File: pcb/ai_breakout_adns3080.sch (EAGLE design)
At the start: 24 parts, among them J1 1X10, U1 VREG-MIC5205-3.3, U2 ADNS-3080, X1 RESON

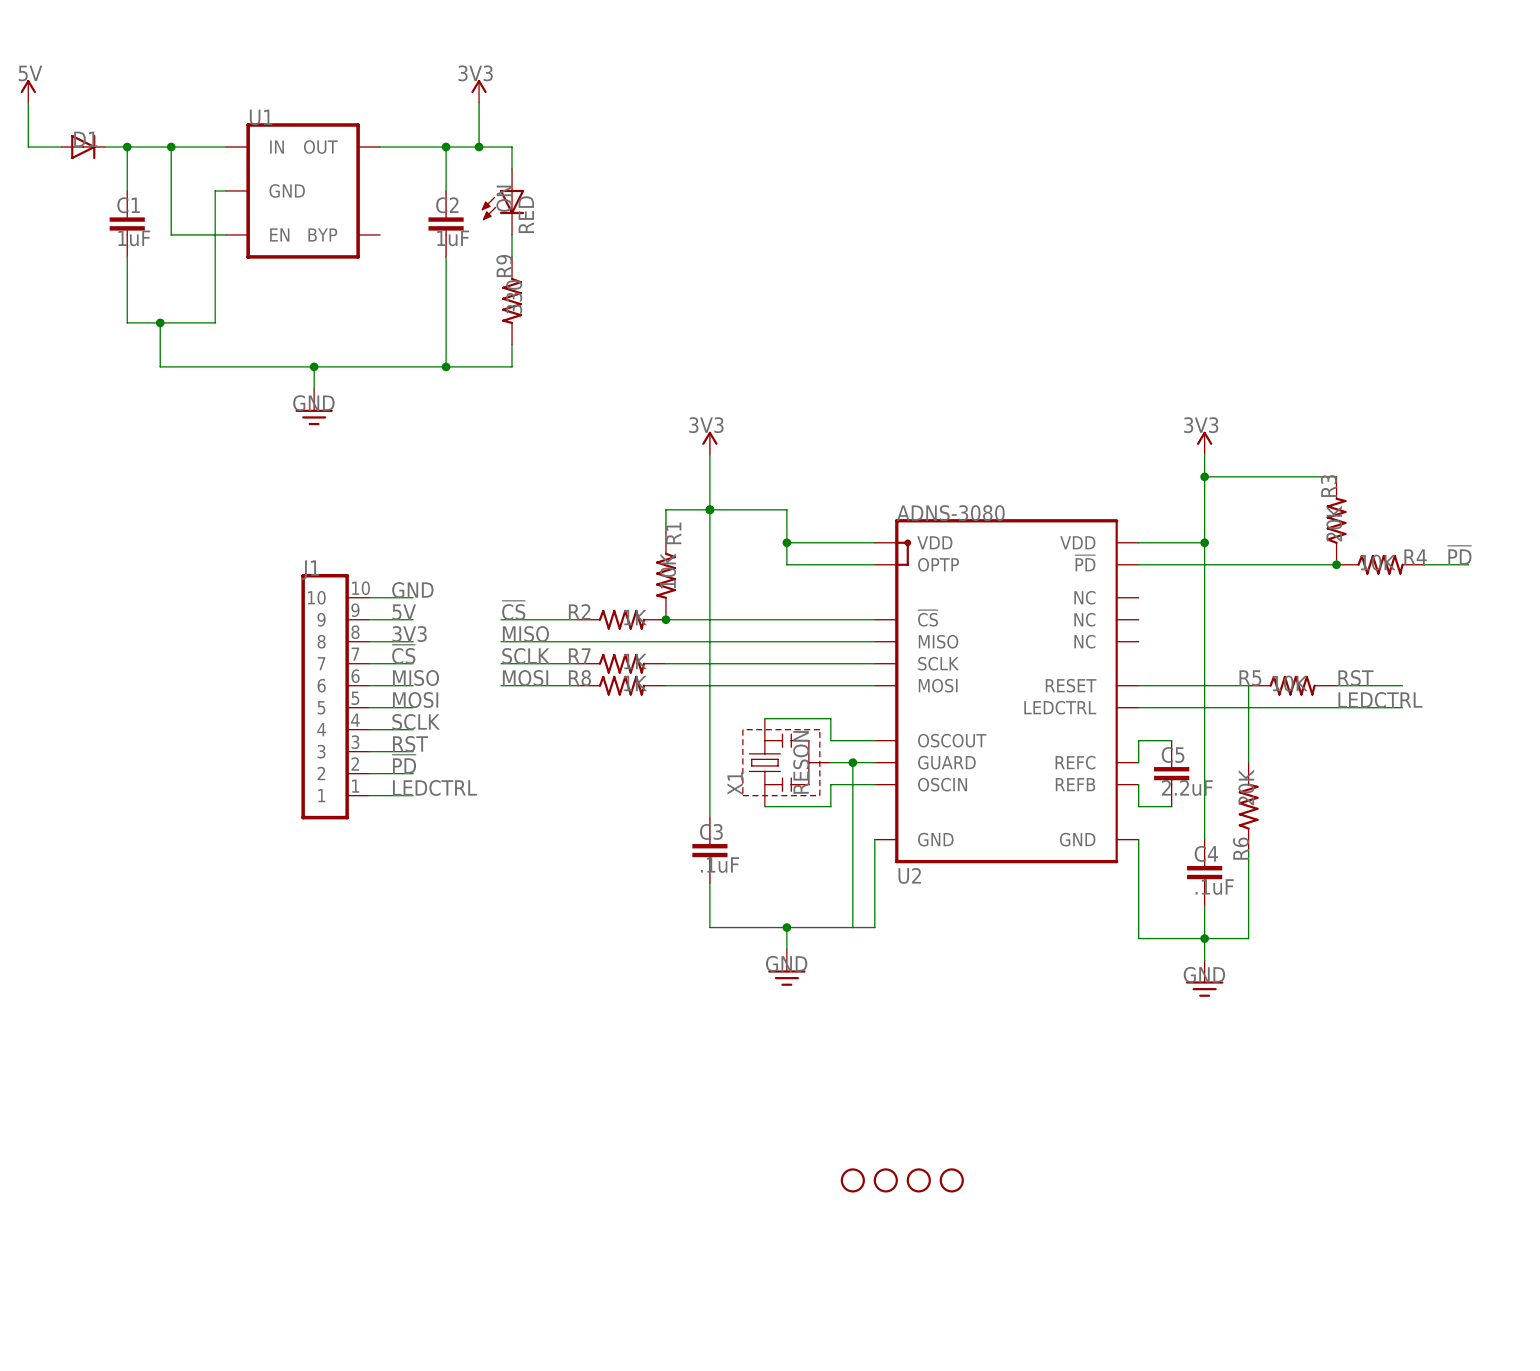
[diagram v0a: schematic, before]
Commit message: Revised version.  Finished BOM.
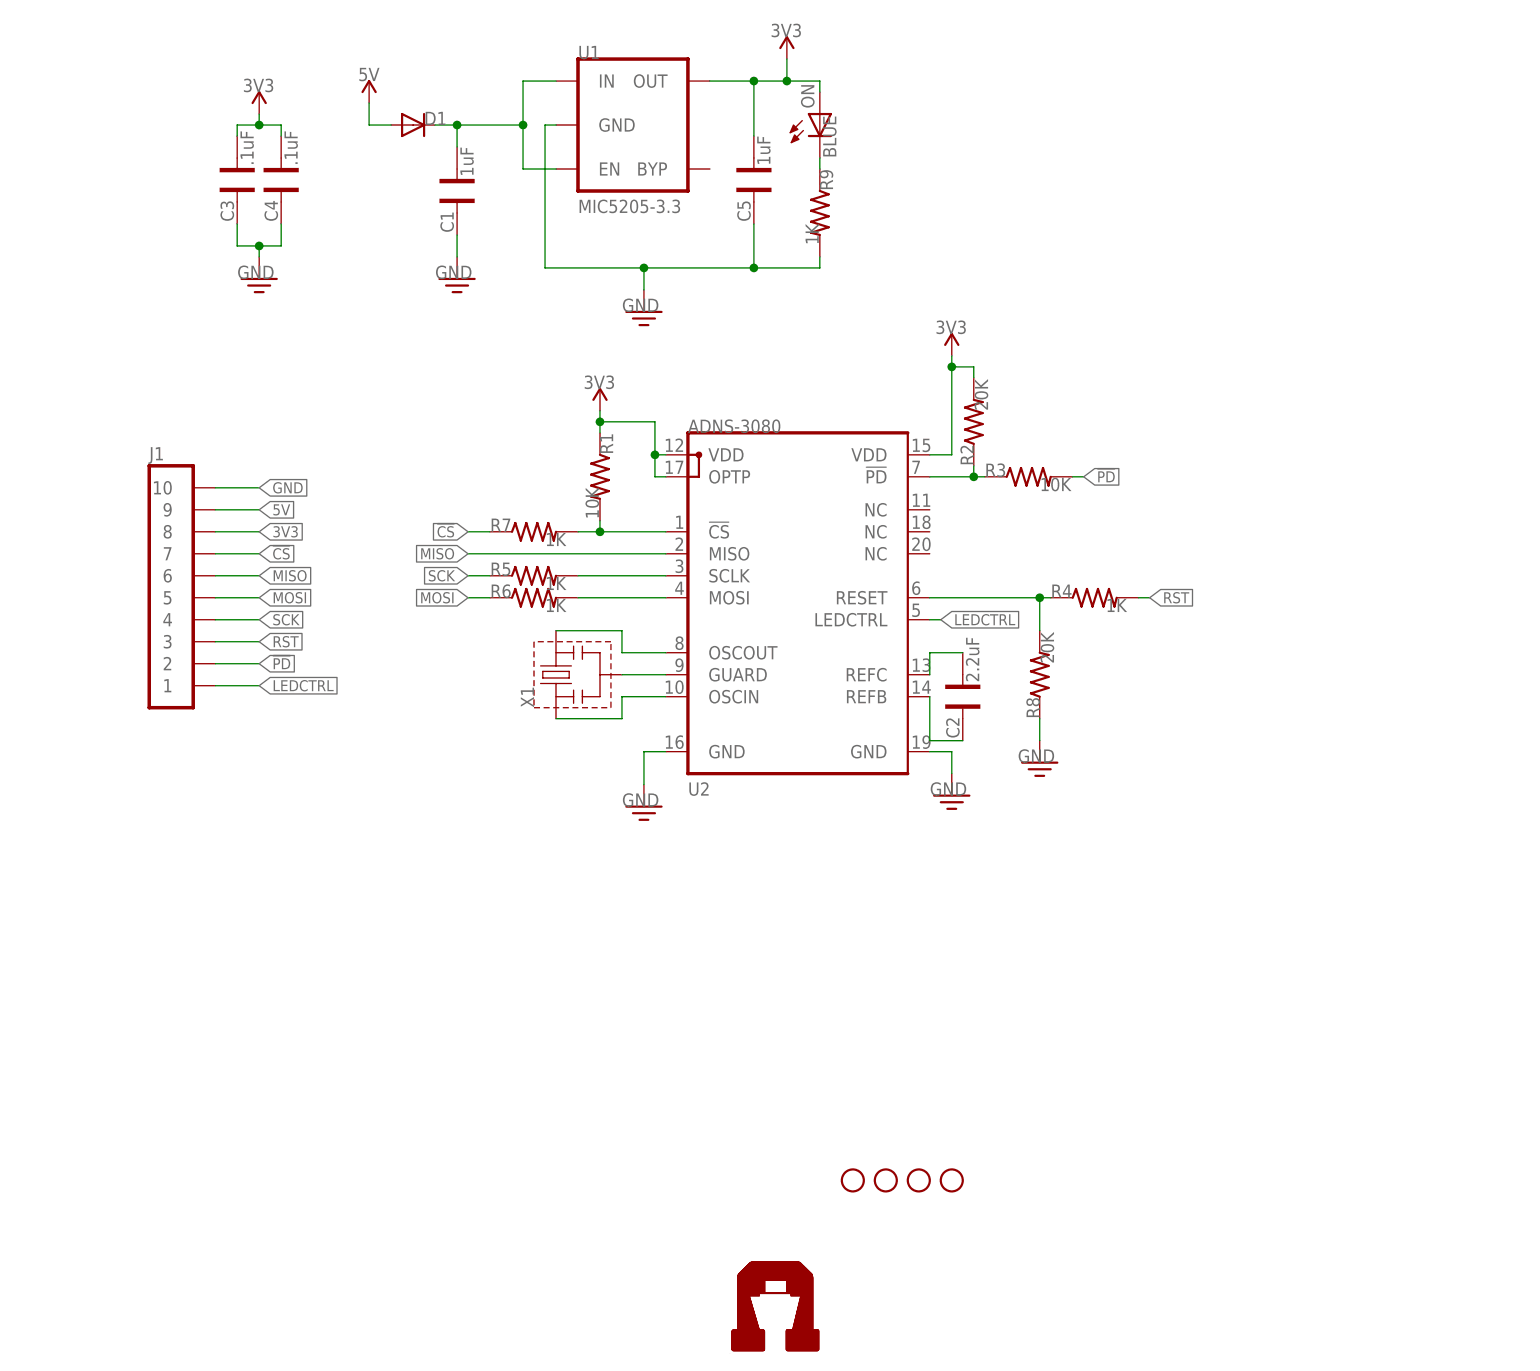
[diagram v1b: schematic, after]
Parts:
- added U$2, U$3: AI-LOGOM, Ai_Miscellany:AI-LOGOM
- C1, C3, C4: device Ai_Passives:CAP -> Ai_Passives:CAP0603
- C2: value 1uF -> 2.2uF; device Ai_Passives:CAP -> Ai_Passives:CAP0603
- C5: value 2.2uF -> 1uF; device Ai_Passives:CAP -> Ai_Passives:CAP0603
- D1: value DIODE -> DIODESMA-403D; device Ai_DiscreteSemis:DIODE -> Ai_DiscreteSemis:DIODESMA-403D
- ON: value RED -> BLUE
- R1, R7: device Ai_Passives:RES -> Ai_Passives:RES0603
- R2, R8: value 1K -> 20K; device Ai_Passives:RES -> Ai_Passives:RES0603
- R3: value 20K -> 10K; device Ai_Passives:RES -> Ai_Passives:RES0603
- R4, R5: value 10K -> 1K; device Ai_Passives:RES -> Ai_Passives:RES0603
- R6: value 20K -> 1K; device Ai_Passives:RES -> Ai_Passives:RES0603
- R9: value 330 -> 1K; device Ai_Passives:RES -> Ai_Passives:RES0603
- U1: value VREG-MIC5205-3.3 -> MIC5205-3.3; device Ai_Power:VREG-MIC5205-3.3 -> Ai_Power:MIC5205-3.3
- X1: value RESON -> RESON025X020; device Ai_Passives:RESON -> Ai_Passives:RESON025X020
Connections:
- removed net N$14: R1.2, R2.2, U2.!CS
- removed net N$18: R3.1, R4.1, U2.!PD
- removed net SCLK: J1.4, R7.1
- new net N$2: U2.GUARD, X1.2
- new net N$4: R1.2, R7.2, U2.!CS
- new net N$7: R2.1, R3.1, U2.!PD
- new net SCK: J1.4, R5.1
- net !CS: now also R7.1; no longer R2.1
- net !PD: now also R3.2; no longer R4.2
- net 3V3: now also C5.1, R2.2; no longer C2.1, R3.2
- net GND: now also C5.2, R8.1; no longer C2.2, R6.1, U2.GUARD, X1.2
- net MOSI: now also R6.1; no longer R8.1
- net N$10: now also R6.2; no longer R8.2
- net N$12: now also R4.1, R8.2; no longer R5.1, R6.2
- net N$16: now also C2.1; no longer C5.1
- net N$17: now also C2.2; no longer C5.2
- net N$5: now also R5.2; no longer R7.2
- net RST: now also R4.2; no longer R5.2
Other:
- moved on the sheet: C1, C2, C3, C4, C5, D1, ON, R1, R2, R3, R4, R5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

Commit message: updating to use the latest libraries
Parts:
- D1: value DIODESMA-403D -> (none)
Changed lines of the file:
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@@
 <setting verticaltext="up"/>
 </settings>
-<grid distance="50" unitdist="mil" unit="mil" style="lines" multiple="1" display="yes" altdistance="0.01" altunitdist="inch" altunit="inch"/>
+<grid distance="0.1" unitdist="inch" unit="inch" style="lines" multiple="1" display="no" altdistance="0.01" altunitdist="inch" altunit="inch"/>
 <layers>
 <layer number="1" name="Top" color="4" fill="1" visible="no" active="no"/>
@@
 <layer number="111" name="circles" color="7" fill="1" visible="yes" active="yes"/>
 <layer number="112" name="hoeken" color="7" fill="1" visible="yes" active="yes"/>
+<layer number="113" name="Route13" color="7" fill="1" visible="no" active="no"/>
 <layer number="116" name="Patch_BOT" color="9" fill="4" visible="yes" active="yes"/>
+<layer number="117" name="mPads" color="7" fill="1" visible="no" active="no"/>
+<layer number="118" name="mVias" color="7" fill="1" visible="no" active="no"/>
+<layer number="119" name="mUnrouted" color="7" fill="1" visible="no" active="no"/>
+<layer number="120" name="mDimension" color="7" fill="1" visible="no" active="no"/>
 <layer number="121" name="_tsilk" color="7" fill="1" visible="yes" active="yes"/>
 <layer number="122" name="_bsilk" color="7" fill="1" visible="yes" active="yes"/>
@@
 <layer number="127" name="_tValues" color="7" fill="1" visible="yes" active="yes"/>
 <layer number="128" name="_bValues" color="7" fill="1" visible="yes" active="yes"/>
+<layer number="129" name="mtStop" color="7" fill="1" visible="no" active="no"/>
+<layer number="130" name="mbStop" color="7" fill="1" visible="no" active="no"/>
 <layer number="131" name="tAdjust" color="7" fill="1" visible="yes" active="yes"/>
 <layer number="132" name="bAdjust" color="7" fill="1" visible="yes" active="yes"/>
+<layer number="133" name="mtFinish" color="7" fill="1" visible="no" active="no"/>
+<layer number="134" name="mbFinish" color="7" fill="1" visible="no" active="no"/>
+<layer number="135" name="mtGlue" color="7" fill="1" visible="no" active="no"/>
+<layer number="136" name="mbGlue" color="7" fill="1" visible="no" active="no"/>
+<layer number="137" name="mtTest" color="7" fill="1" visible="no" active="no"/>
+<layer number="138" name="mbTest" color="7" fill="1" visible="no" active="no"/>
+<layer number="139" name="mtKeepout" color="7" fill="1" visible="no" active="no"/>
+<layer number="140" name="mbKeepout" color="7" fill="1" visible="no" active="no"/>
+<layer number="141" name="mtRestrict" color="7" fill="1" visible="no" active="no"/>
+<layer number="142" name="mbRestrict" color="7" fill="1" visible="no" active="no"/>
+<layer number="143" name="mvRestrict" color="7" fill="1" visible="no" active="no"/>
 <layer number="144" name="Drill_legend" color="7" fill="1" visible="yes" active="yes"/>
+<layer number="145" name="mHoles" color="7" fill="1" visible="no" active="no"/>
+<layer number="146" name="mMilling" color="7" fill="1" visible="no" active="no"/>
+<layer number="147" name="mMeasures" color="7" fill="1" visible="no" active="no"/>
+<layer number="148" name="mDocument" color="7" fill="1" visible="no" active="no"/>
+<layer number="149" name="mReference" color="7" fill="1" visible="no" active="no"/>
 <layer number="150" name="Notes" color="7" fill="1" visible="no" active="yes"/>
 <layer number="151" name="HeatSink" color="7" fill="1" visible="yes" active="yes"/>
@@
 <layer number="154" name="FabDoc2" color="2" fill="1" visible="no" active="no"/>
 <layer number="155" name="FabDoc3" color="7" fill="15" visible="no" active="no"/>
+<layer number="191" name="mNets" color="7" fill="1" visible="no" active="no"/>
+<layer number="192" name="mBusses" color="7" fill="1" visible="no" active="no"/>
+<layer number="193" name="mPins" color="7" fill="1" visible="no" active="no"/>
+<layer number="194" name="mSymbols" color="7" fill="1" visible="no" active="no"/>
+<layer number="195" name="mNames" color="7" fill="1" visible="no" active="no"/>
+<layer number="196" name="mValues" color="7" fill="1" visible="no" active="no"/>
 <layer number="199" name="PSR2000 hulplijn" color="14" fill="1" visible="yes" active="yes"/>
 <layer number="200" name="200bmp" color="1" fill="10" visible="no" active="no"/>
